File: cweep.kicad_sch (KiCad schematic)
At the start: 73 parts, among them J1 24AWG Hole, J2 24AWG Hole, SW1 SW_Push, SW10 SW_Push, SW11 SW_Push, SW12 SW_Push, SW13 SW_Push, SW14 SW_Push, SW15 SW_Push, SW16 SW_Push, SW17 SW_Push, SW18 SW_SPST, SW19 SW_Omron_B3FS, SW2 SW_Push, SW3 SW_Push, SW4 SW_Push, SW5 SW_Push, SW6 SW_Push, SW7 SW_Push, SW8 SW_Push, SW9 SW_Push, U1 XIAO-nRF52840, U2 BQ25504RGTR

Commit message: feat: make remaining components reversible
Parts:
- BT1: footprint com_snapeda_Keystone:BatteryHolder_Keystone_230-1_1x10440 -> cweep:BatteryHolder_Keystone_230-1_1x10440
- H1, H2, H3, H4, H5, H6: footprint MountingHole:MountingHole_2.2mm_M2_DIN965_Pad_TopOnly -> cweep:MountingHole_2.2mm_M2_DIN965_Pad
- SW18: footprint KAN-15:SW_KAN-15_PHT -> cweep:SW_KAN-15_PHT_Reversible
- SW19: footprint Button_Switch_THT:SW_TH_Tactile_Omron_B3F-10xx -> cweep:SW_TH_Tactile_Omron_B3F-10xx_Reversible
- U1: footprint Seeed Studio XIAO Series Library:XIAO-nRF52840 -> cweep:XIAO-nRF52840_Reversible
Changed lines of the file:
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@@
 			)
 		)
-		(property "Footprint" "MountingHole:MountingHole_2.2mm_M2_DIN965_Pad_TopOnly"
+		(property "Footprint" "cweep:MountingHole_2.2mm_M2_DIN965_Pad"
 			(at 20.32 137.16 0)
 			(effects
@@
 			)
 		)
-		(property "Footprint" "KAN-15:SW_KAN-15_PHT"
+		(property "Footprint" "cweep:SW_KAN-15_PHT_Reversible"
 			(at 55.88 158.75 0)
 			(effects
@@
 			)
 		)
-		(property "Footprint" "com_snapeda_Keystone:BatteryHolder_Keystone_230-1_1x10440"
+		(property "Footprint" "cweep:BatteryHolder_Keystone_230-1_1x10440"
 			(at 55.626 135.89 90)
 			(effects
@@
 			)
 		)
-		(property "Footprint" "MountingHole:MountingHole_2.2mm_M2_DIN965_Pad_TopOnly"
+		(property "Footprint" "cweep:MountingHole_2.2mm_M2_DIN965_Pad"
 			(at 20.32 109.22 0)
 			(effects
@@
 			)
 		)
-		(property "Footprint" "MountingHole:MountingHole_2.2mm_M2_DIN965_Pad_TopOnly"
+		(property "Footprint" "cweep:MountingHole_2.2mm_M2_DIN965_Pad"
 			(at 20.32 128.27 0)
 			(effects
@@
 			)
 		)
-		(property "Footprint" "Button_Switch_THT:SW_TH_Tactile_Omron_B3F-10xx"
+		(property "Footprint" "cweep:SW_TH_Tactile_Omron_B3F-10xx_Reversible"
 			(at 55.88 109.22 0)
 			(effects
@@
 			)
 		)
-		(property "Footprint" "MountingHole:MountingHole_2.2mm_M2_DIN965_Pad_TopOnly"
+		(property "Footprint" "cweep:MountingHole_2.2mm_M2_DIN965_Pad"
 			(at 20.32 146.05 0)
 			(effects
@@
 			)
 		)
-		(property "Footprint" "Seeed Studio XIAO Series Library:XIAO-nRF52840"
+		(property "Footprint" "cweep:XIAO-nRF52840_Reversible"
 			(at 98.6633 132.08 0)
 			(effects
@@
 			)
 		)
-		(property "Footprint" "MountingHole:MountingHole_2.2mm_M2_DIN965_Pad_TopOnly"
+		(property "Footprint" "cweep:MountingHole_2.2mm_M2_DIN965_Pad"
 			(at 20.32 119.38 0)
 			(effects
@@
 			)
 		)
-		(property "Footprint" "MountingHole:MountingHole_2.2mm_M2_DIN965_Pad_TopOnly"
+		(property "Footprint" "cweep:MountingHole_2.2mm_M2_DIN965_Pad"
 			(at 20.32 154.94 0)
 			(effects

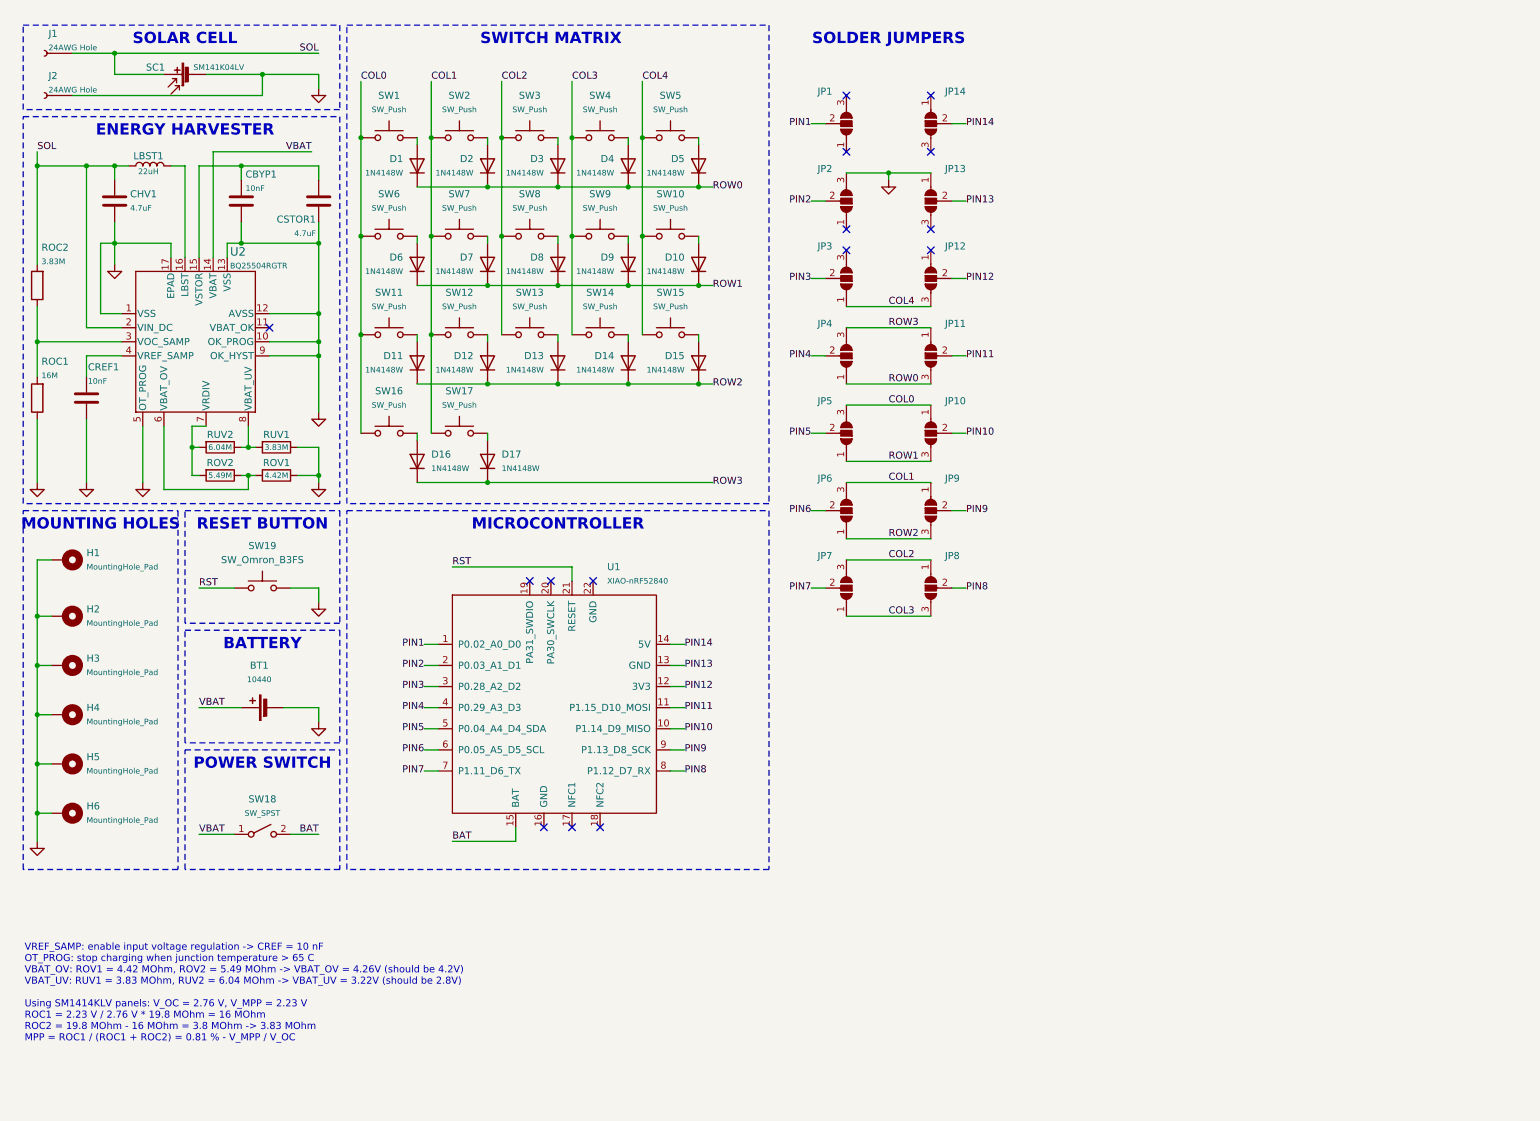
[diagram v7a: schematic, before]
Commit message: refactor: use kicad libraries for BQ25504
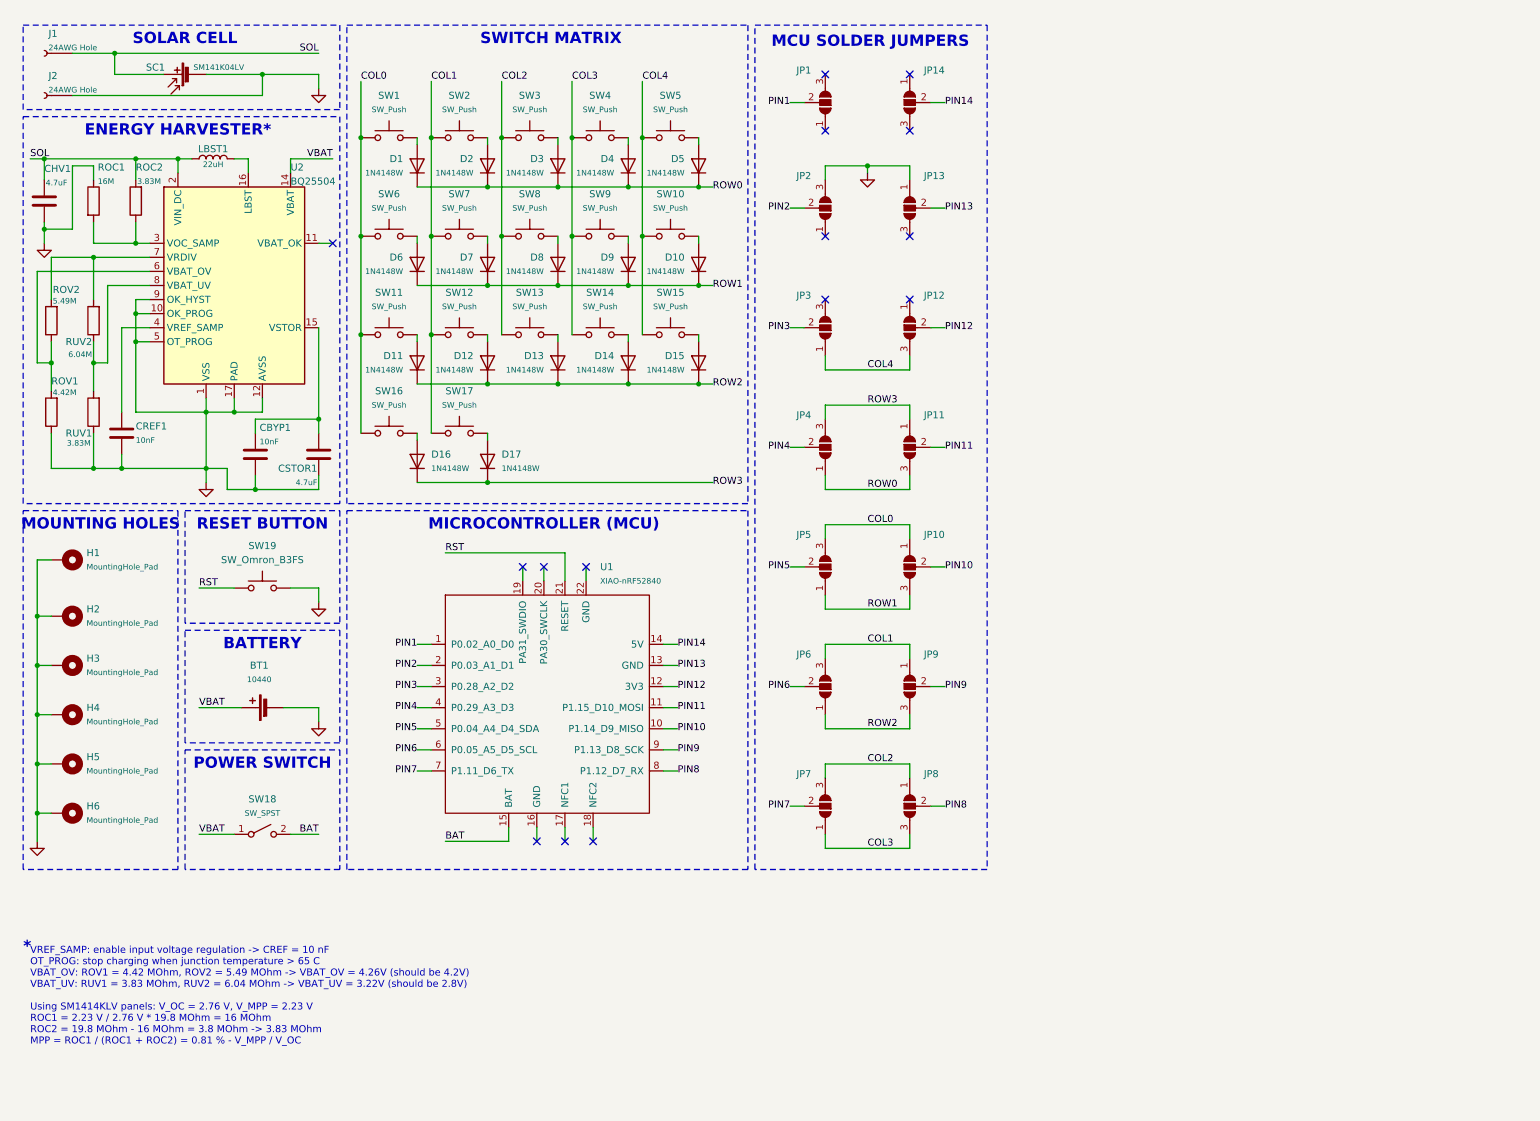
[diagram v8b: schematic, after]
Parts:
- SC1: symbol Device:Solar_Cell -> cweep:Solar_Cell
- U2: value BQ25504RGTR -> BQ25504; footprint BQ25504RGTR:RGT16_1P7X1P7 -> Package_DFN_QFN:VQFN-16-1EP_3x3mm_P0.5mm_EP1.68x1.68mm; symbol BQ25504RGTR:BQ25504RGTR -> Battery_Management:BQ25504
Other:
- note added: "*"
- note added: "ENERGY HARVESTER*"
- note added: "MCU SOLDER JUMPERS"
- note added: "MICROCONTROLLER (MCU)"
- note removed: "ENERGY HARVESTER"
- note removed: "MICROCONTROLLER"
- note removed: "SOLDER JUMPERS"
- moved on the sheet: CBYP1, CHV1, CREF1, CSTOR1, JP1, JP10, JP11, JP12, JP13, JP14, JP2, JP3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
